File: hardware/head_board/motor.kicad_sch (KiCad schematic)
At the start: 18 parts, among them J4 MOTOR, U7 TMC2209

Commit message: v1 revision to the schematic
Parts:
- added FB? (x4): 50Ω @ 100MHz / 2A, symbol Device:FerriteBead_Small
- added R?: 10K, Resistor_SMD:R_0402_1005Metric_Pad0.72x0.64mm_HandSolder, symbol Device:R_US
- added RV? (x2): 35V, symbol Device:Varistor
- R17, R4: value 22R -> 220m
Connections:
- net +3V3: now also R?.2
- net ENN: now also R?.1
- net at C48.1, J4.2 (Pin_2): now also FB?.2, RV?.2; no longer U7.26 (OB1)
- net at C46.1, J4.4 (Pin_4): now also FB?.2, RV?.2; no longer U7.21 (OA2)
- net at C49.1, J4.1 (Pin_1): now also FB?.2, RV?.1; no longer U7.1 (OB2)
- net at C47.1, J4.3 (Pin_3): now also FB?.2, RV?.1; no longer U7.24 (OA1)
- new net: FB?.1, U7.26 (OB1)
- new net: FB?.1, U7.1 (OB2)
- new net: FB?.1, U7.21 (OA2)
- new net: FB?.1, U7.24 (OA1)
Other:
- note added: "* Maximum current limited to 1 A(RMS) with R(sense) R4, R17 at 220mΩ * ESD & EME circuitry per Datasheet 3.7 * Bypass capacitors per Datasheet 3.1 * Internal clock set by CLK pulled low * SPREAD left floating since configuration is done via UART"
- note added: "Motor driver"
- note added: "Motor power supply bypassing"
- note added: "Protection circuitry"
- note removed: "Capacitor values per Datasheet 3.1"
- note removed: "Capacitors at driver outputs for EME per Datasheet 3.7"
- note removed: "Internal CLK"
- note removed: "SpreadCycle/StealthChop configured via UART"
- company: (none) -> Winterbloom
- title: (none) -> Candela Head
- moved on the sheet: C36, C37, C38, C39, C40, C41, C42, C43, C44, C45, C46, C47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

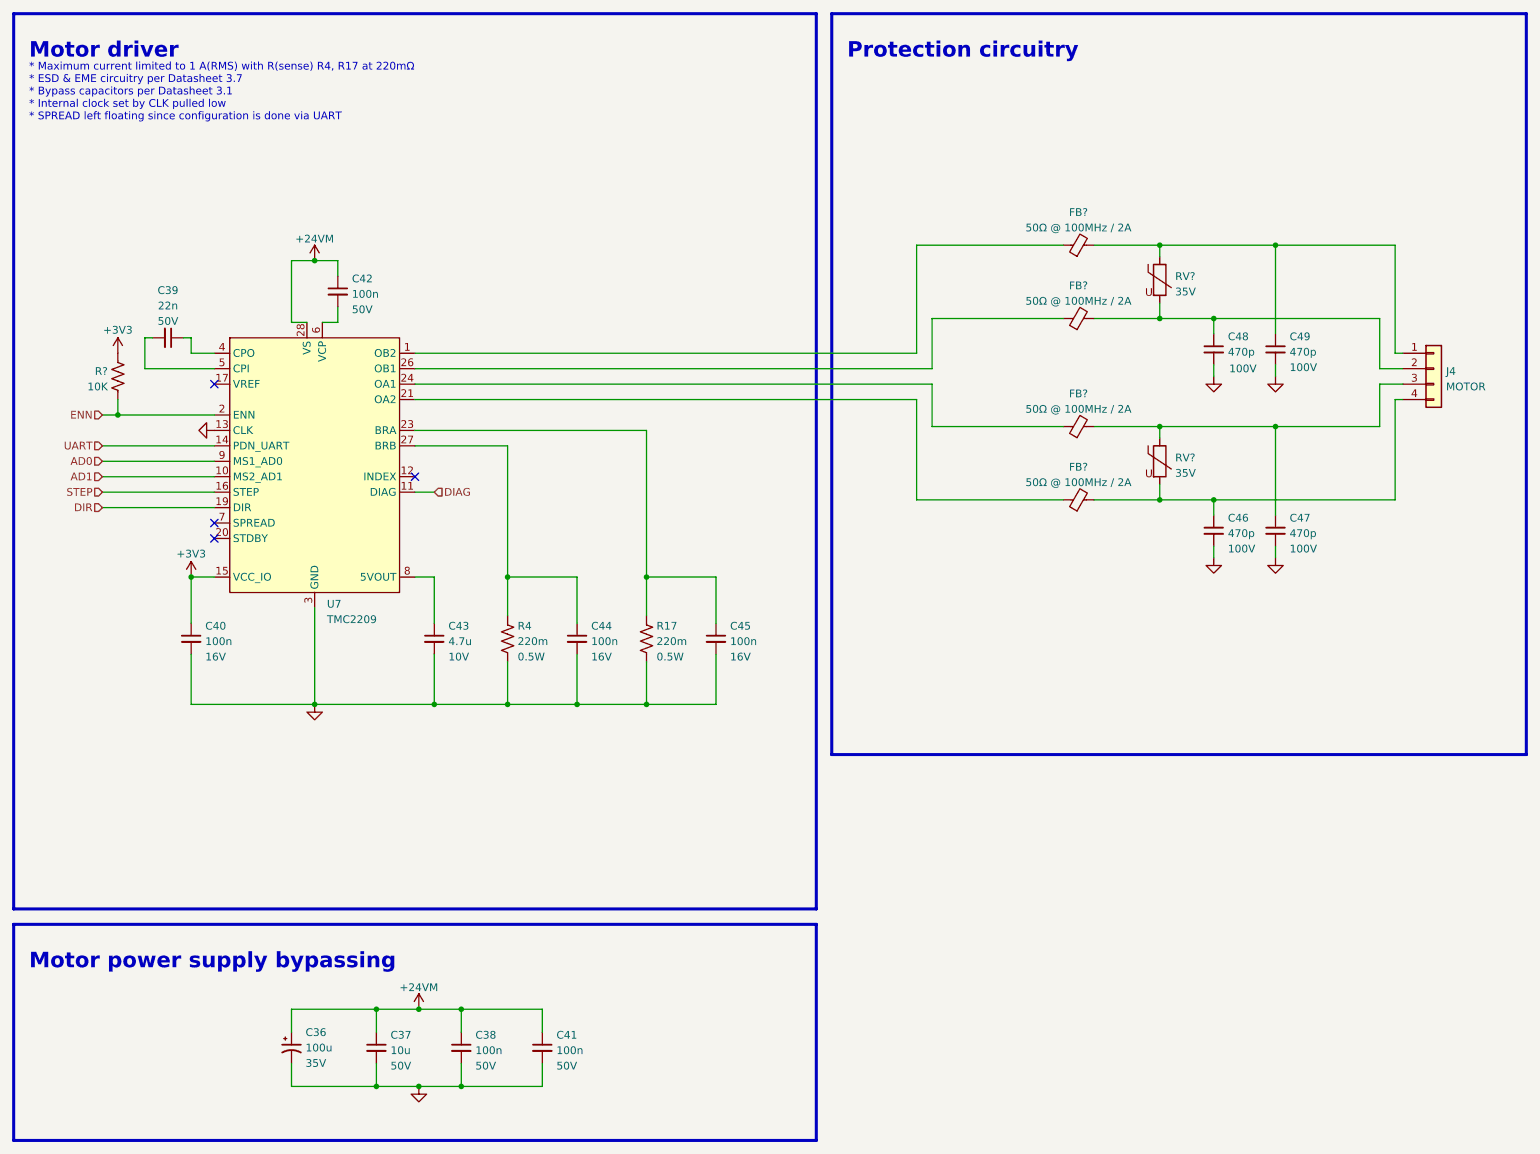
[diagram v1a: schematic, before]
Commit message: Footprints assigned
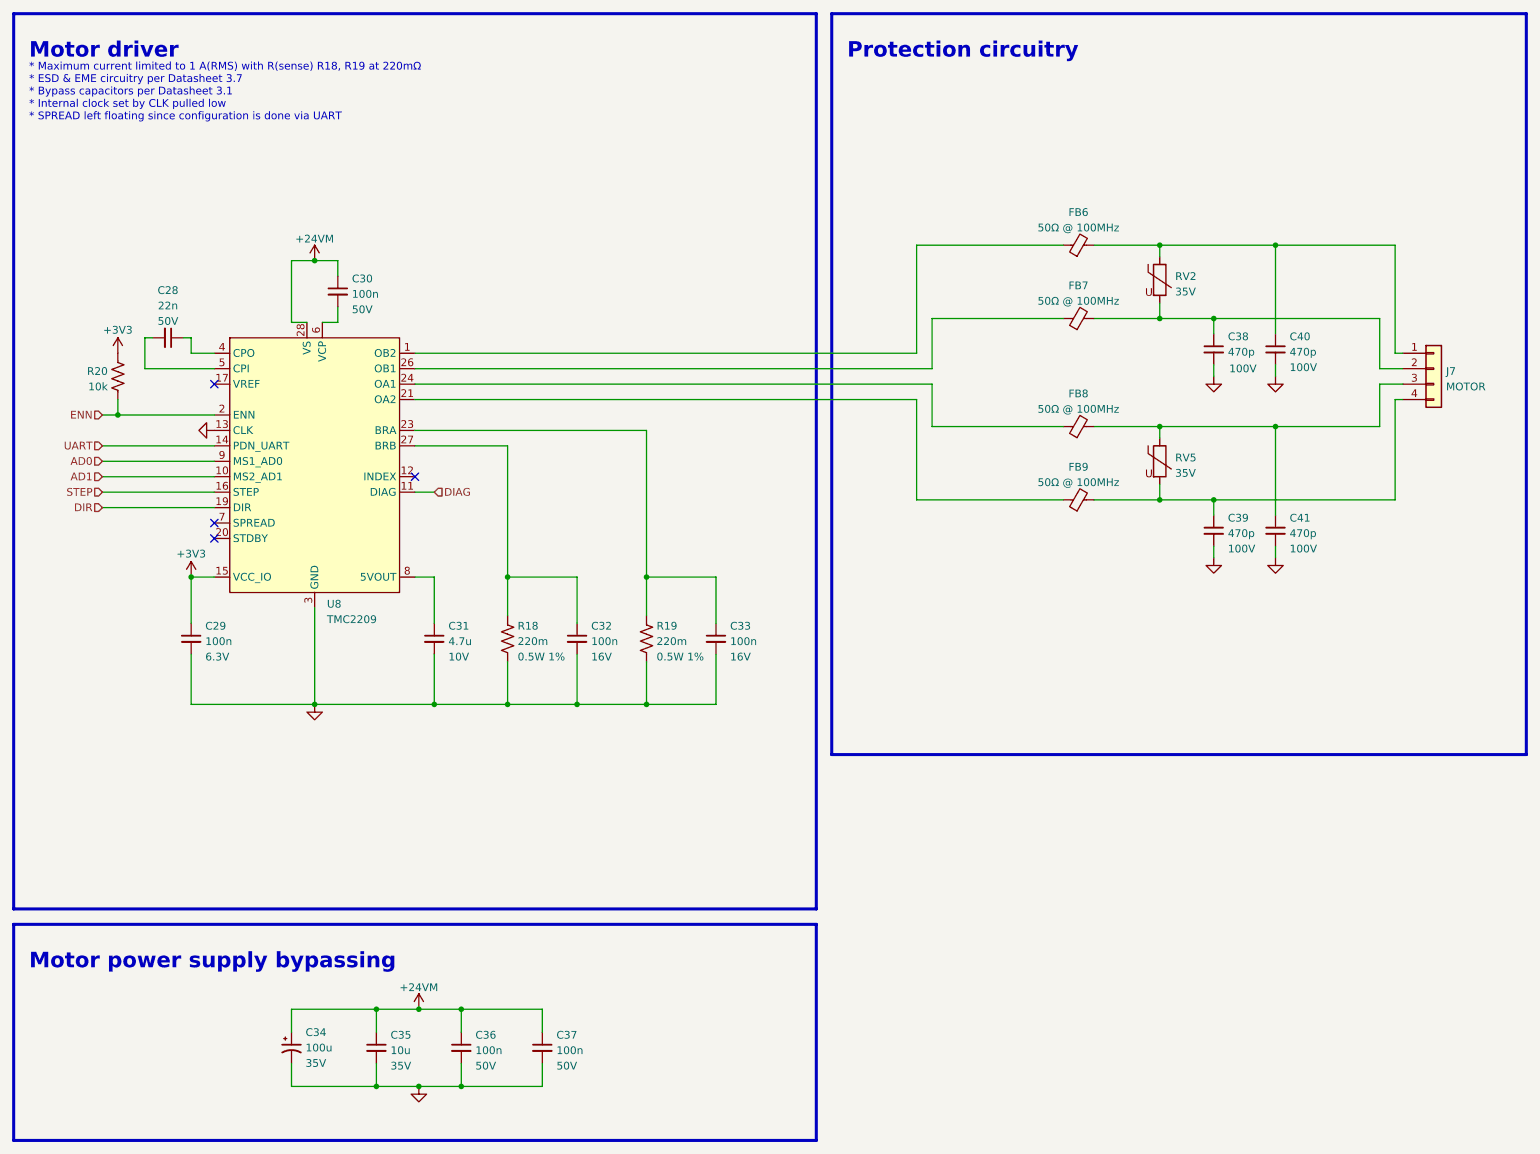
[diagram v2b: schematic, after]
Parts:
- C29: renamed from C40; Rating 16V -> 6.3V
- C35: renamed from C37; Rating 50V -> 35V
- FB6, FB7, FB8, FB9: renamed from FB?; value 50Ω @ 100MHz / 2A -> 50Ω @ 100MHz; footprint (none) -> Inductor_SMD:L_0603_1608Metric_Pad1.05x0.95mm_HandSolder; Rating (none) -> 2A; mpn (none) -> BLM18KG121TN1D
- R18: renamed from R4; Rating 0.5W -> 0.5W 1%
- R19: renamed from R17; Rating 0.5W -> 0.5W 1%
- R20: renamed from R?; value 10K -> 10k; Rating (none) -> 63mW
- RV2, RV5: renamed from RV?; footprint (none) -> Resistor_SMD:R_0603_1608Metric_Pad0.98x0.95mm_HandSolder; mpn (none) -> B72500D0300H060
- renumbered C39 to C28, C42 to C30, C43 to C31, C44 to C32, C45 to C33, C36 to C34, C38 to C36, C41 to C37, C48 to C38, C46 to C39, C49 to C40, C47 to C41, J4 to J7, U7 to U8
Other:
- note added: "* Maximum current limited to 1 A(RMS) with R(sense) R18, R19 at 220mΩ * ESD & EME circuitry per Datasheet 3.7 * Bypass capacitors per Datasheet 3.1 * Internal clock set by CLK pulled low * SPREAD left floating since configuration is done via UART"
- note removed: "* Maximum current limited to 1 A(RMS) with R(sense) R4, R17 at 220mΩ * ESD & EME circuitry per Datasheet 3.7 * Bypass capacitors per Datasheet 3.1 * Internal clock set by CLK pulled low * SPREAD left floating since configuration is done via UART"

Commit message: Finish up layout for v1, ended up removing some stuff
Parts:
- removed C34: 100u, Capacitor_SMD:CP_Elec_6.3x7.7, symbol Device:C_Polarized_Small_US
- C31: mpn CL10A475KP8NNNC -> CL10A475KP8NNNC
- R18, R19: mpn RCS120622R0FKEA -> KDV12DR240ET
- renumbered FB6 to FB2, FB7 to FB3, FB8 to FB4, FB9 to FB5, R20 to R17, RV5 to RV3
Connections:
- net at C41.1, FB4.2, RV3.1: now also J7.2 (Pin_2); no longer J7.3 (Pin_3)
- net at C39.1, FB5.2, RV3.2: now also J7.1 (Pin_1); no longer J7.4 (Pin_4)
- net at C38.1, FB3.2, RV2.2: now also J7.3 (Pin_3); no longer J7.2 (Pin_2)
- net OB1: now reaches FB3.1, U8.26 (OB1)
- net OB2: now reaches FB2.1, U8.1 (OB2)
- net OA2: now reaches FB5.1, U8.21 (OA2)
- net OA1: now reaches FB4.1, U8.24 (OA1)
- net at C40.1, FB2.2, RV2.1: now also J7.4 (Pin_4); no longer J7.1 (Pin_1)
- net +24V renamed VS

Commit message: V2 of the head board (Jellyfish)
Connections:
- net BRA: now reaches C33.1, R19.2, U8.23 (BRA)
- net CPO: now reaches C28.1, U8.4 (CPO)
- net CPI: now reaches C28.2, U8.5 (CPI)
- net 5VOUT: now reaches C31.1, U8.8 (5VOUT)
- net BRB: now reaches C32.1, R18.2, U8.27 (BRB)
- net VCP: now reaches C30.2, U8.6 (VCP)
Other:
- title: Candela Head -> Jellyfish
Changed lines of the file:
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@@
   (paper "USLetter")
   (title_block
-    (title "Candela Head")
-    (date "2022-07-27")
-    (rev "v1")
+    (title "Jellyfish")
+    (date "2022-09-07")
+    (rev "v2")
     (company "Winterbloom")
     (comment 1 "Alethea Flowers")
     (comment 2 "CERN-OHL-P V2")
+    (comment 3 "jellyfish.wntr.dev")
   )
   (junction (at 212.725 95.25) (diameter 0) (color 0 0 0 0)
@@
     (effects (font (size 1.27 1.27)) (justify left bottom))
   )
+  (label "CPI" (at 48.26 73.66 180)
+    (effects (font (size 0.64 0.64)) (justify right bottom))
+  )
+  (label "BRA" (at 81.28 83.82 0)
+    (effects (font (size 0.64 0.64)) (justify left bottom))
+  )
+  (label "5VOUT" (at 81.28 107.95 0)
+    (effects (font (size 0.64 0.64)) (justify left bottom))
+  )
+  (label "BRB" (at 81.28 86.36 0)
+    (effects (font (size 0.64 0.64)) (justify left bottom))
+  )
   (label "OA1" (at 89.535 76.2 0)
     (effects (font (size 1.27 1.27)) (justify left bottom))
   )
+  (label "VCP" (at 68.58 66.04 0)
+    (effects (font (size 0.64 0.64)) (justify left bottom))
+  )
   (label "OA2" (at 89.535 78.74 0)
     (effects (font (size 1.27 1.27)) (justify left bottom))
@@
     (effects (font (size 1.27 1.27)) (justify left bottom))
   )
+  (label "CPO" (at 48.26 71.12 180)
+    (effects (font (size 0.64 0.64)) (justify right bottom))
+  )
   (global_label "VMOTOR" (shape input) (at 64.77 55.88 90) (fields_autoplaced)
